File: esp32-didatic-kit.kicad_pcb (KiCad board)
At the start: 2 copper layers, 266 x 220 mm, 0 parts

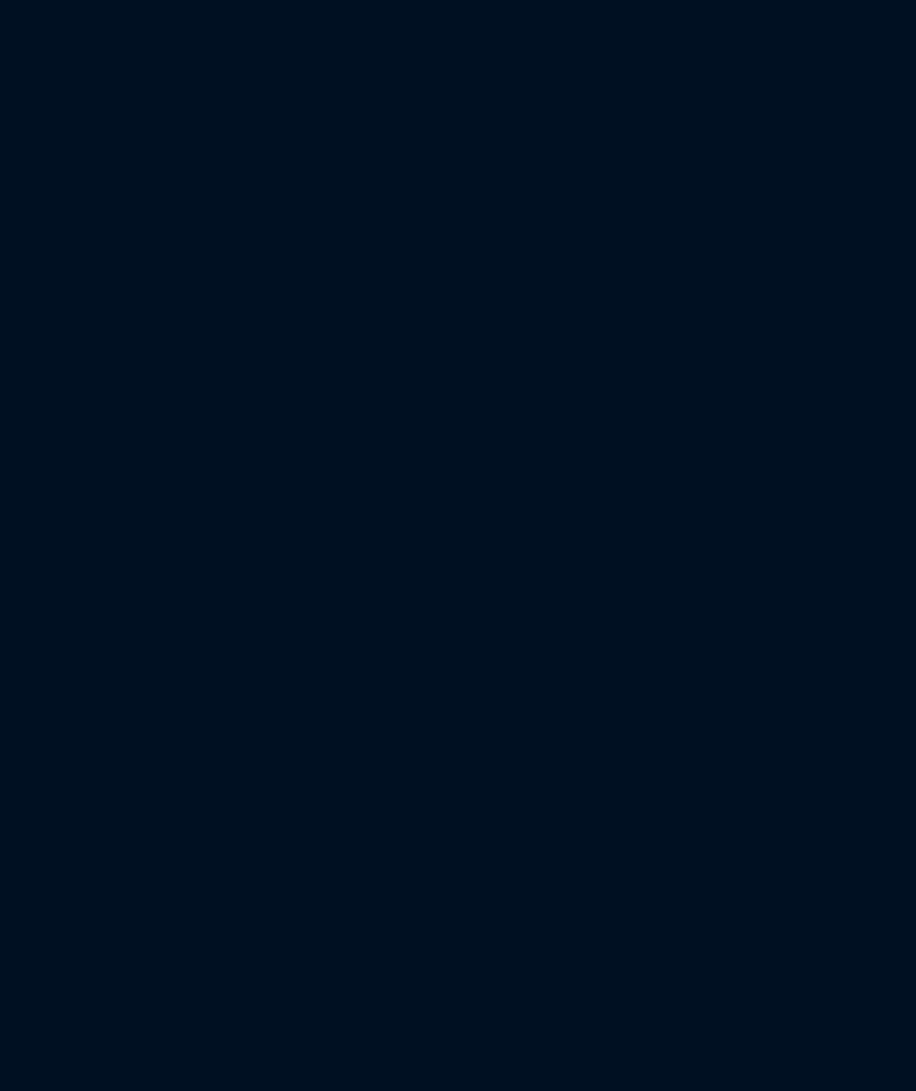
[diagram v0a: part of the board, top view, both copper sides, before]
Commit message: Use kicad footprints
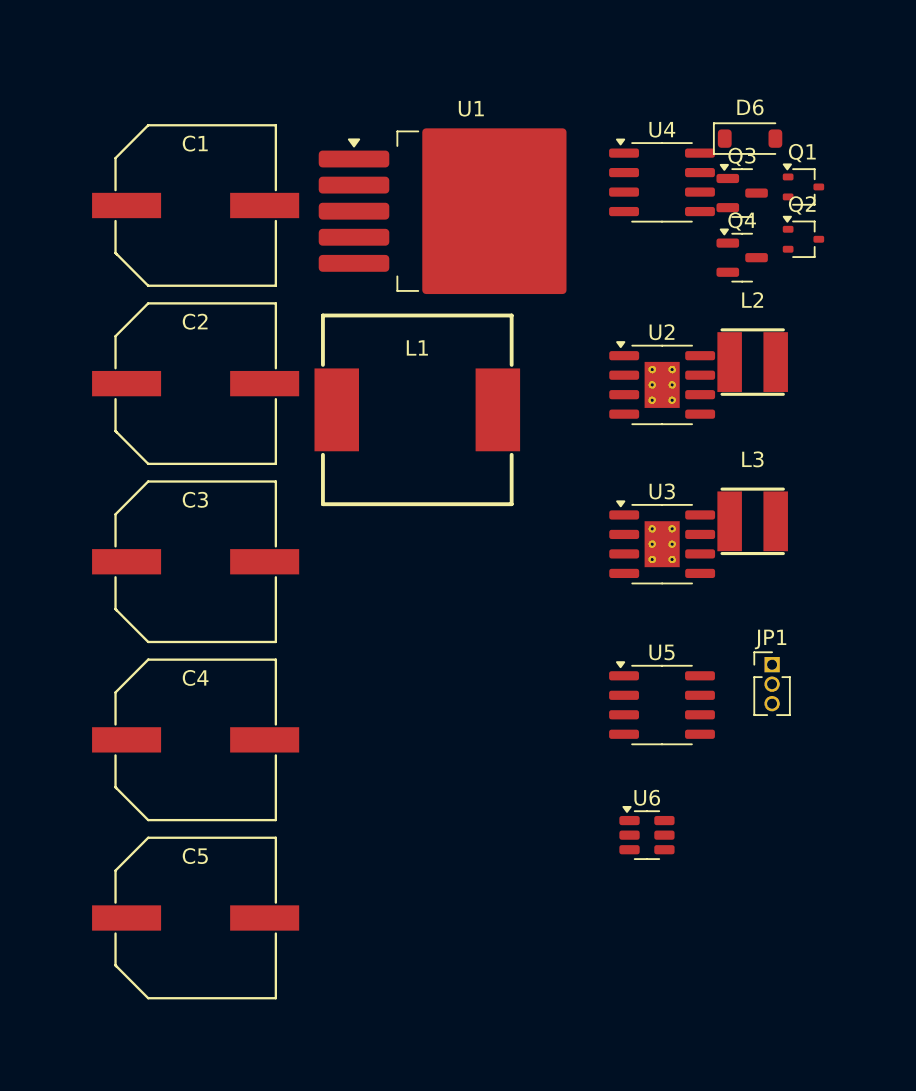
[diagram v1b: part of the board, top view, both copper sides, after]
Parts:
- added C1: 330uF, Passive:CAP-SMD_BD10.0-L10.3-W10.3-LS10.9-FD, F.Cu at (286.4, 61.3)
- added C2: 330uF, Passive:CAP-SMD_BD10.0-L10.3-W10.3-LS10.9-FD, F.Cu at (286.4, 72.9)
- added C3: 330uF, Passive:CAP-SMD_BD10.0-L10.3-W10.3-LS10.9-FD, F.Cu at (286.4, 84.5)
- added C4: 330uF, Passive:CAP-SMD_BD10.0-L10.3-W10.3-LS10.9-FD, F.Cu at (286.4, 96.1)
- added C5: 330uF, Passive:CAP-SMD_BD10.0-L10.3-W10.3-LS10.9-FD, F.Cu at (286.4, 107.7)
- added D6: PMEG3010ER,115, Diode_SMD:D_SOD-123, F.Cu at (322.6, 56.9)
- added JP1: REF-SEL, Connector_PinHeader_1.27mm:PinHeader_1x03_P1.27mm_Vertical, F.Cu at (324.0, 91.2)
- added L1: SMDRI127-221MT, Passive:IND-SMD_L12.3-W12.3_SMDRI127, F.Cu at (300.9, 74.6)
- added L2: 10uH, Passive:IND-SMD_L4.0-W4.0_FNR40XXS, F.Cu at (322.7, 71.5)
- added L3: 10uH, Passive:IND-SMD_L4.0-W4.0_FNR40XXS, F.Cu at (322.7, 81.9)
- added Q1: PDTC114EU,115, Package_TO_SOT_SMD:SOT-323_SC-70, F.Cu at (326.0, 60.1)
- added Q2: DMP2160UW-7, Package_TO_SOT_SMD:SOT-323_SC-70, F.Cu at (326.0, 63.5)
- added Q3: DMN2058U-7, Package_TO_SOT_SMD:SOT-23, F.Cu at (322.0, 60.5)
- added Q4: DMN2058U-7, Package_TO_SOT_SMD:SOT-23, F.Cu at (322.0, 64.7)
- added U1: LM2575-12BU, Package_TO_SOT_SMD:TO-263-5_TabPin3, F.Cu at (304.4, 61.6)
- added U2: ST1S10PHR, Package_SO:SOIC-8-1EP_3.9x4.9mm_P1.27mm_EP2.29x3mm_ThermalVias, F.Cu at (316.8, 73.0)
- added U3: ST1S10PHR, Package_SO:SOIC-8-1EP_3.9x4.9mm_P1.27mm_EP2.29x3mm_ThermalVias, F.Cu at (316.8, 83.3)
- added U4: MCP6H02T-E/SN, Package_SO:SOIC-8_3.9x4.9mm_P1.27mm, F.Cu at (316.8, 59.8)
- added U5: MCP1501-40E/SN, Package_SO:SOIC-8_3.9x4.9mm_P1.27mm, F.Cu at (316.8, 93.8)
- added U6: MCP4726A0T-E/CH, Package_TO_SOT_SMD:SOT-23-6, F.Cu at (315.8, 102.3)

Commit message: add MCU + output
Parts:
- added D10: LL4148, Diode_SMD:D_MiniMELF, F.Cu at (279.4, 182.0)
- added D11: LL4148, Diode_SMD:D_MiniMELF, F.Cu at (292.9, 178.7)
- added D12: LL4148, Diode_SMD:D_MiniMELF, F.Cu at (292.9, 182.0)
- added D13: LL4148, Diode_SMD:D_MiniMELF, F.Cu at (279.4, 197.6)
- added D14: LL4148, Diode_SMD:D_MiniMELF, F.Cu at (279.4, 200.9)
- added D15: LL4148, Diode_SMD:D_MiniMELF, F.Cu at (306.4, 178.7)
- added D16: LL4148, Diode_SMD:D_MiniMELF, F.Cu at (306.4, 182.0)
- added D17: LL4148, Diode_SMD:D_MiniMELF, F.Cu at (265.8, 178.7)
- added D18: LL4148, Diode_SMD:D_MiniMELF, F.Cu at (265.8, 182.0)
- added D19: LL4148, Diode_SMD:D_MiniMELF, F.Cu at (306.4, 197.6)
- added D20: LL4148, Diode_SMD:D_MiniMELF, F.Cu at (306.4, 200.9)
- added D21: LL4148, Diode_SMD:D_MiniMELF, F.Cu at (292.9, 197.6)
- added D22: LL4148, Diode_SMD:D_MiniMELF, F.Cu at (292.9, 200.9)
- added D23: LL4148, Diode_SMD:D_MiniMELF, F.Cu at (265.8, 197.6)
- added D24: LL4148, Diode_SMD:D_MiniMELF, F.Cu at (265.8, 200.9)
- added D8: LL4148, Diode_SMD:D_MiniMELF, F.Cu at (218.2, 151.2)
- added D9: LL4148, Diode_SMD:D_MiniMELF, F.Cu at (279.4, 178.7)
- added J2: Conn_02x05_Odd_Even, Connector_PinHeader_2.54mm:PinHeader_2x05_P2.54mm_Vertical, F.Cu at (264.9, 152.3)
- added J3: Conn_02x05_Odd_Even, Connector_PinHeader_2.54mm:PinHeader_2x05_P2.54mm_Vertical, F.Cu at (287.0, 152.3)
- added J4: Conn_02x05_Odd_Even, Connector_PinHeader_2.54mm:PinHeader_2x05_P2.54mm_Vertical, F.Cu at (287.0, 135.6)
- added J5: Conn_02x05_Odd_Even, Connector_PinHeader_2.54mm:PinHeader_2x05_P2.54mm_Vertical, F.Cu at (264.9, 135.6)
- added K1: G2RL-1, Relay_THT:Relay_SPDT_Omron_G2RL-1, F.Cu at (132.2, 35.1)
- added K10: G2RL-1, Relay_THT:Relay_SPDT_Omron_G2RL-1, F.Cu at (164.6, 100.0)
- added K11: G2RL-1, Relay_THT:Relay_SPDT_Omron_G2RL-1, F.Cu at (196.9, 100.0)
- added K12: G2RL-1, Relay_THT:Relay_SPDT_Omron_G2RL-1, F.Cu at (180.7, 67.5)
- added K13: G2RL-1, Relay_THT:Relay_SPDT_Omron_G2RL-1, F.Cu at (180.7, 100.0)
- added K14: G2RL-1, Relay_THT:Relay_SPDT_Omron_G2RL-1, F.Cu at (109.2, 69.7)
- added K15: G2RL-1, Relay_THT:Relay_SPDT_Omron_G2RL-1, F.Cu at (164.6, 67.5)
- added K16: G2RL-1, Relay_THT:Relay_SPDT_Omron_G2RL-1, F.Cu at (196.9, 67.5)
- added K2: G2RL-1, Relay_THT:Relay_SPDT_Omron_G2RL-1, F.Cu at (196.9, 35.1)
- added K3: G2RL-1, Relay_THT:Relay_SPDT_Omron_G2RL-1, F.Cu at (132.2, 67.5)
- added K4: G2RL-1, Relay_THT:Relay_SPDT_Omron_G2RL-1, F.Cu at (148.4, 67.5)
- added K5: G2RL-1, Relay_THT:Relay_SPDT_Omron_G2RL-1, F.Cu at (132.2, 100.0)
- added K6: G2RL-1, Relay_THT:Relay_SPDT_Omron_G2RL-1, F.Cu at (164.6, 35.1)
- added K7: G2RL-1, Relay_THT:Relay_SPDT_Omron_G2RL-1, F.Cu at (148.4, 35.1)
- added K8: G2RL-1, Relay_THT:Relay_SPDT_Omron_G2RL-1, F.Cu at (180.7, 35.1)
- added K9: G2RL-1, Relay_THT:Relay_SPDT_Omron_G2RL-1, F.Cu at (148.4, 100.0)
- added Q5: BSS138, Package_TO_SOT_SMD:SOT-23, F.Cu at (242.6, 198.3)
- added Q6: BSS138, Package_TO_SOT_SMD:SOT-23, F.Cu at (242.6, 202.9)
- added R30: 4K7, Resistor_SMD:R_0603_1608Metric, F.Cu at (238.2, 197.1)
- added R31: 4K7, Resistor_SMD:R_0603_1608Metric, F.Cu at (238.2, 199.7)
- added R32: 4K7, Resistor_SMD:R_0603_1608Metric, F.Cu at (238.2, 202.2)
- added R33: 4K7, Resistor_SMD:R_0603_1608Metric, F.Cu at (238.2, 204.7)
- added SW6: SW_DIP_x08, Button_Switch_SMD:SW_DIP_SPSTx08_Slide_6.7x21.88mm_W6.73mm_P2.54mm_LowProfile_JPin, F.Cu at (256.8, 49.7)
- added SW7: SW_DIP_x08, Button_Switch_SMD:SW_DIP_SPSTx08_Slide_6.7x21.88mm_W6.73mm_P2.54mm_LowProfile_JPin, F.Cu at (273.7, 49.8)
- added TB1: MKDSN 1,5/ 2-5,08, TerminalBlock_Phoenix:TerminalBlock_Phoenix_MKDS-1,5-2-5.08_1x02_P5.08mm_Horizontal, F.Cu at (239.7, 139.5)
- added TB10: MKDSN 1,5/ 2-5,08, TerminalBlock_Phoenix:TerminalBlock_Phoenix_MKDS-1,5-2-5.08_1x02_P5.08mm_Horizontal, F.Cu at (252.0, 188.0)
- added TB2: MKDSN 1,5/ 2-5,08, TerminalBlock_Phoenix:TerminalBlock_Phoenix_MKDS-1,5-2-5.08_1x02_P5.08mm_Horizontal, F.Cu at (239.7, 151.6)
- added TB3: MKDSN 1,5/ 2-5,08, TerminalBlock_Phoenix:TerminalBlock_Phoenix_MKDS-1,5-2-5.08_1x02_P5.08mm_Horizontal, F.Cu at (239.7, 163.8)
- added TB4: MKDSN 1,5/ 2-5,08, TerminalBlock_Phoenix:TerminalBlock_Phoenix_MKDS-1,5-2-5.08_1x02_P5.08mm_Horizontal, F.Cu at (239.7, 175.9)
- added TB5: MKDSN 1,5/ 2-5,08, TerminalBlock_Phoenix:TerminalBlock_Phoenix_MKDS-1,5-2-5.08_1x02_P5.08mm_Horizontal, F.Cu at (239.7, 188.0)
- added TB6: MKDSN 1,5/ 2-5,08, TerminalBlock_Phoenix:TerminalBlock_Phoenix_MKDS-1,5-2-5.08_1x02_P5.08mm_Horizontal, F.Cu at (252.0, 139.5)
- added TB7: MKDSN 1,5/ 2-5,08, TerminalBlock_Phoenix:TerminalBlock_Phoenix_MKDS-1,5-2-5.08_1x02_P5.08mm_Horizontal, F.Cu at (252.0, 151.6)
- added TB8: MKDSN 1,5/ 2-5,08, TerminalBlock_Phoenix:TerminalBlock_Phoenix_MKDS-1,5-2-5.08_1x02_P5.08mm_Horizontal, F.Cu at (252.0, 163.8)
- added TB9: MKDSN 1,5/ 2-5,08, TerminalBlock_Phoenix:TerminalBlock_Phoenix_MKDS-1,5-2-5.08_1x02_P5.08mm_Horizontal, F.Cu at (252.0, 175.9)
- added U10: HCPL2630SDVM, ICs:PDIP-8_L9.6-W6.4-P2.54-LS7.9-BL, F.Cu at (295.8, 171.9)
- added U11: HCPL2630SDVM, ICs:PDIP-8_L9.6-W6.4-P2.54-LS7.9-BL, F.Cu at (282.2, 190.8)
- added U12: HCPL2630SDVM, ICs:PDIP-8_L9.6-W6.4-P2.54-LS7.9-BL, F.Cu at (309.3, 171.9)
- added U13: HCPL2630SDVM, ICs:PDIP-8_L9.6-W6.4-P2.54-LS7.9-BL, F.Cu at (268.7, 171.9)
- added U14: HCPL2630SDVM, ICs:PDIP-8_L9.6-W6.4-P2.54-LS7.9-BL, F.Cu at (309.3, 190.8)
- added U15: HCPL2630SDVM, ICs:PDIP-8_L9.6-W6.4-P2.54-LS7.9-BL, F.Cu at (295.8, 190.8)
- added U16: HCPL2630SDVM, ICs:PDIP-8_L9.6-W6.4-P2.54-LS7.9-BL, F.Cu at (268.7, 190.8)
- added U17: PCF8574AT, Package_SO:SOIC-16W_7.5x10.3mm_P1.27mm, F.Cu at (298.3, 156.1)
- added U18: PCF8574AT, Package_SO:SOIC-16W_7.5x10.3mm_P1.27mm, F.Cu at (298.3, 139.3)
- added U19: PCF8574AT, Package_SO:SOIC-16W_7.5x10.3mm_P1.27mm, F.Cu at (276.2, 139.3)
- added U20: ULN2803A, Package_SO:SOIC-18W_7.5x11.6mm_P1.27mm, F.Cu at (112.3, 105.7)
- added U21: ULN2803A, Package_SO:SOIC-18W_7.5x11.6mm_P1.27mm, F.Cu at (102.6, 130.0)
- added U7: ESP32-WROVER-B, ICs:MODULE_ESP32-WROVER-B, F.Cu at (154.2, 172.0)
- added U8: PCF8574AT, Package_SO:SOIC-16W_7.5x10.3mm_P1.27mm, F.Cu at (276.2, 156.1)
- added U9: HCPL2630SDVM, ICs:PDIP-8_L9.6-W6.4-P2.54-LS7.9-BL, F.Cu at (282.2, 171.9)
- renumbered Q2 to Q1, Q1 to Q2, U6 to U5, U5 to U6
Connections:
- C1 pad 2: GND -> +5V
- C2 pad 2: GND -> +5V
- C3 pad 2: GND -> +5V
- C4 pad 2: GND -> +5V
- C5 pad 2: GND -> +5V
- Q2 pad 2: GND -> +5V
- Q3 pad 2: GND -> +5V
- Q4 pad 2: GND -> +5V
- U1 pad 3: GND -> +5V
- U2 pad 4: GND -> +5V
- U2 pad 5: GND -> +5V
- U2 pad 8: GND -> +5V
- U2 pad 9: GND -> +5V
- U3 pad 4: GND -> +5V
- U3 pad 5: GND -> +5V
- U3 pad 8: GND -> +5V
- U3 pad 9: GND -> +5V
- U4 pad 4: GND -> +5V
- U5 pad 2: GND -> +5V
- U6 pad 2: GND -> +5V
- U6 pad 4: GND -> +5V
- U6 pad 5: GND -> +5V
- U6 pad 6: GND -> +5V

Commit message: add mcu module + position components
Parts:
- removed Q6: BSS138, Package_TO_SOT_SMD:SOT-23
- removed R30, R31, R32, R33: 4K7, Resistor_SMD:R_0603_1608Metric
- added BOOT1: TL3342F160QG, Button_Switch_SMD:SW_SPST_TL3342, F.Cu at (486.6, 63.4)
- added C38: 30pF 50v, Capacitor_SMD:C_0603_1608Metric, F.Cu at (436.2, 129.5)
- added C39: 100nF, Capacitor_SMD:C_0603_1608Metric, F.Cu at (436.2, 132.0)
- added C40: 30pF 50v, Capacitor_SMD:C_0603_1608Metric, F.Cu at (436.2, 134.5)
- added C41: 30pF 50v, Capacitor_SMD:C_0603_1608Metric, F.Cu at (436.2, 137.0)
- added C48: 10nF, Capacitor_SMD:C_0603_1608Metric, F.Cu at (493.3, 64.5)
- added C49: 10nF, Capacitor_SMD:C_0603_1608Metric, F.Cu at (493.3, 67.0)
- added CON1: MIKROBUS_HOST_CONN, Connectors:MIKROBUS_HOST_CONN, F.Cu at (101.3, 100.1)
- added CON2: MIKROBUS_HOST_CONN, Connectors:MIKROBUS_HOST_CONN, F.Cu at (101.3, 129.7)
- added CON3: MIKROBUS_HOST_CONN, Connectors:MIKROBUS_HOST_CONN, F.Cu at (101.3, 160.1)
- added D41: BAT54J, Diode_SMD:D_SOD-323F, F.Cu at (448.9, 145.4)
- added J6: USB_C_Receptacle, Connector_USB:USB_C_Receptacle_GCT_USB4105-xx-A_16P_TopMnt_Horizontal, F.Cu at (440.1, 109.9)
- added J8: MCU_MODULE_CONN, Connectors:mcu_conn, F.Cu at (209.3, 136.4)
- added JP2: Jumper_3_Open, Connector_PinHeader_2.54mm:PinHeader_1x03_P2.54mm_Vertical, F.Cu at (484.1, 52.5)
- added JP3: Jumper_3_Open, Connector_PinHeader_2.54mm:PinHeader_1x03_P2.54mm_Vertical, F.Cu at (488.7, 52.5)
- added JP4: Jumper_3_Open, Connector_PinHeader_2.54mm:PinHeader_1x03_P2.54mm_Vertical, F.Cu at (493.3, 52.5)
- added JP5: Jumper_3_Open, Connector_PinHeader_2.54mm:PinHeader_1x03_P2.54mm_Vertical, F.Cu at (497.9, 52.5)
- added JP6: SolderJumper_2_Open, Jumper:SolderJumper-2_P1.3mm_Open_RoundedPad1.0x1.5mm, F.Cu at (448.9, 142.1)
- added Q7: 2N7002, Package_TO_SOT_SMD:SOT-23, F.Cu at (448.9, 69.9)
- added R103: 2K, Resistor_SMD:R_0603_1608Metric, F.Cu at (436.2, 139.5)
- added R104: 4K7, Resistor_SMD:R_0603_1608Metric, F.Cu at (436.2, 142.1)
- added R105: 4K7, Resistor_SMD:R_0603_1608Metric, F.Cu at (436.2, 144.6)
- added R106: 5K1, Resistor_SMD:R_0603_1608Metric, F.Cu at (444.7, 120.5)
- added R107: 5K1, Resistor_SMD:R_0603_1608Metric, F.Cu at (444.7, 123.0)
- added R35: 4K7, Resistor_SMD:R_0603_1608Metric, F.Cu at (448.4, 54.1)
- added R36: 4K7, Resistor_SMD:R_0603_1608Metric, F.Cu at (448.4, 56.6)
- added R37: 4K7, Resistor_SMD:R_0603_1608Metric, F.Cu at (448.4, 59.1)
- added R38: 4K7, Resistor_SMD:R_0603_1608Metric, F.Cu at (448.4, 61.6)
- added RST1: TL3342F160QG, Button_Switch_SMD:SW_SPST_TL3342, F.Cu at (486.6, 70.5)
- added SW2: TDS08SGRNTU04, Connectors:TDS08SGRNTU04, F.Cu at (315.6, 92.7)
- added SW3: TDS08SGRNTU04, Connectors:TDS08SGRNTU04, F.Cu at (315.7, 147.8)
- added SW4: TDS08SGRNTU04, Connectors:TDS08SGRNTU04, F.Cu at (274.9, 149.1)
- added SW5: TDS08SGRNTU04, Connectors:TDS08SGRNTU04, F.Cu at (272.7, 92.5)
- added TB11: MKDSN 1,5/ 2-5,08, TerminalBlock_Phoenix:TerminalBlock_Phoenix_MKDS-1,5-2-5.08_1x02_P5.08mm_Horizontal, F.Cu at (441.8, 134.5)
- added TB13: MKDSN 1,5/ 2-5,08, TerminalBlock_Phoenix:TerminalBlock_Phoenix_MKDS-1,5-2-5.08_1x02_P5.08mm_Horizontal, F.Cu at (110.3, 238.9)
- added TB14: MKDSN 1,5/ 2-5,08, TerminalBlock_Phoenix:TerminalBlock_Phoenix_MKDS-1,5-2-5.08_1x02_P5.08mm_Horizontal, F.Cu at (227.4, 238.9)
- added TB15: MKDSN 1,5/ 2-5,08, TerminalBlock_Phoenix:TerminalBlock_Phoenix_MKDS-1,5-2-5.08_1x02_P5.08mm_Horizontal, F.Cu at (122.0, 238.9)
- added TB16: MKDSN 1,5/ 2-5,08, TerminalBlock_Phoenix:TerminalBlock_Phoenix_MKDS-1,5-2-5.08_1x02_P5.08mm_Horizontal, F.Cu at (239.1, 238.9)
- added TB17: MKDSN 1,5/ 2-5,08, TerminalBlock_Phoenix:TerminalBlock_Phoenix_MKDS-1,5-2-5.08_1x02_P5.08mm_Horizontal, F.Cu at (133.7, 238.9)
- added TB18: MKDSN 1,5/ 2-5,08, TerminalBlock_Phoenix:TerminalBlock_Phoenix_MKDS-1,5-2-5.08_1x02_P5.08mm_Horizontal, F.Cu at (250.8, 238.9)
- added TB19: MKDSN 1,5/ 2-5,08, TerminalBlock_Phoenix:TerminalBlock_Phoenix_MKDS-1,5-2-5.08_1x02_P5.08mm_Horizontal, F.Cu at (145.4, 238.9)
- added TB20: MKDSN 1,5/ 2-5,08, TerminalBlock_Phoenix:TerminalBlock_Phoenix_MKDS-1,5-2-5.08_1x02_P5.08mm_Horizontal, F.Cu at (262.5, 238.9)
- added TB21: MKDSN 1,5/ 2-5,08, TerminalBlock_Phoenix:TerminalBlock_Phoenix_MKDS-1,5-2-5.08_1x02_P5.08mm_Horizontal, F.Cu at (157.1, 238.9)
- added TB22: MKDSN 1,5/ 2-5,08, TerminalBlock_Phoenix:TerminalBlock_Phoenix_MKDS-1,5-2-5.08_1x02_P5.08mm_Horizontal, F.Cu at (274.2, 238.9)
- added TB23: MKDSN 1,5/ 2-5,08, TerminalBlock_Phoenix:TerminalBlock_Phoenix_MKDS-1,5-2-5.08_1x02_P5.08mm_Horizontal, F.Cu at (168.8, 238.9)
- added TB24: MKDSN 1,5/ 2-5,08, TerminalBlock_Phoenix:TerminalBlock_Phoenix_MKDS-1,5-2-5.08_1x02_P5.08mm_Horizontal, F.Cu at (285.9, 238.9)
- added TB25: MKDSN 1,5/ 2-5,08, TerminalBlock_Phoenix:TerminalBlock_Phoenix_MKDS-1,5-2-5.08_1x02_P5.08mm_Horizontal, F.Cu at (180.5, 238.9)
- added TB26: MKDSN 1,5/ 2-5,08, TerminalBlock_Phoenix:TerminalBlock_Phoenix_MKDS-1,5-2-5.08_1x02_P5.08mm_Horizontal, F.Cu at (297.6, 238.9)
- added TB27: MKDSN 1,5/ 2-5,08, TerminalBlock_Phoenix:TerminalBlock_Phoenix_MKDS-1,5-2-5.08_1x02_P5.08mm_Horizontal, F.Cu at (192.2, 238.9)
- added TB28: MKDSN 1,5/ 2-5,08, TerminalBlock_Phoenix:TerminalBlock_Phoenix_MKDS-1,5-2-5.08_1x02_P5.08mm_Horizontal, F.Cu at (309.3, 238.9)
- added TB29: MKDSN 1,5/ 2-5,08, TerminalBlock_Phoenix:TerminalBlock_Phoenix_MKDS-1,5-2-5.08_1x02_P5.08mm_Horizontal, F.Cu at (332.7, 238.9)
- added TB30: MKDSN 1,5/ 2-5,08, TerminalBlock_Phoenix:TerminalBlock_Phoenix_MKDS-1,5-2-5.08_1x02_P5.08mm_Horizontal, F.Cu at (321.0, 238.9)
- added TB31: MKDSN 1,5/ 2-5,08, TerminalBlock_Phoenix:TerminalBlock_Phoenix_MKDS-1,5-2-5.08_1x02_P5.08mm_Horizontal, F.Cu at (203.9, 238.9)
- added TB32: MKDSN 1,5/ 2-5,08, TerminalBlock_Phoenix:TerminalBlock_Phoenix_MKDS-1,5-2-5.08_1x02_P5.08mm_Horizontal, F.Cu at (215.7, 238.9)
- added U22: SN65HVD231, Package_SO:SOIC-8_3.9x4.9mm_P1.27mm, F.Cu at (442.5, 143.7)
- added U23: USBLC6-2SC6, Package_TO_SOT_SMD:SOT-23-6, F.Cu at (445.2, 117.0)
- added U24: CH340G, Package_SO:SOIC-16_3.9x9.9mm_P1.27mm, F.Cu at (438.4, 120.5)
- Q5: value BSS138 -> 2N7002
- moved U7 330.7 mm to (476.8, 245.1)
- moved D8 290.6 mm to (494.6, 61.6)
- moved Q5 245.4 mm to (448.9, 65.2)
- moved TB10 227.7 mm to (83.0, 35.4)
- moved D19 226.6 mm to (129.6, 55.9)
- moved D20 226.6 mm to (129.6, 59.2)
- moved U14 226.6 mm to (132.4, 49.1)
- moved D21 225.2 mm to (117.8, 55.9)
- moved D22 225.2 mm to (117.8, 59.2)
- moved U15 225.2 mm to (120.7, 49.1)
- moved D23 213.2 mm to (106.1, 56.3)
- moved D24 213.2 mm to (106.1, 59.6)
- moved U16 213.2 mm to (109.0, 49.5)
- moved TB9 210.9 mm to (94.7, 35.4)
- moved K14 200.5 mm to (271.0, 188.2)
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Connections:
- net /MCU/GPIO25 renamed /MCU/VSPI.CS0
- net /MCU/GPIO26 renamed /MCU/VSPI.CS1
- net /MCU/GPIO32 renamed /MCU/IO32
- net /MCU/GPIO33 renamed /MCU/IO33
- net /MCU/JTAG.TDI renamed Net-(D8-A)
- net /MCU/SERIAL0.IO0 renamed /USB-SERIAL/DBG_UART.DTR
- K10 pad 12: /IO/Output PortD/Relay Circuit1/NC -> /IO/Output PortD/NC1
- K10 pad 14: /IO/Output PortD/Relay Circuit1/NO -> /IO/Output PortD/NO1
- K2 pad 12: /IO/Output PortC/Relay Circuit1/NC -> /IO/Output PortC/NC1
- K2 pad 14: /IO/Output PortC/Relay Circuit1/NO -> /IO/Output PortC/NO1
- Q5 pad 2: /IO/IO_SDA -> /MCU/I2C0.SCL
- Q5 pad 3: /IO/I2C.SDA -> /IO/I2C.SCL
- U7 pad 12: /MCU/GPIO27 -> unconnected-(U7-IO27-Pad12)
- U7 pad 13: /MCU/JTAG.TMS -> Net-(JP3-C)
- U7 pad 16: /MCU/JTAG.TCK -> Net-(JP4-C)
- U7 pad 23: /MCU/JTAG.TDO -> /MCU/IO15
- U7 pad 24: /MCU/GPIO2 -> unconnected-(U7-IO2-Pad24)
- U7 pad 26: /MCU/GPIO4 -> /Can Bus/CAN.RX
- U7 pad 29: /MCU/GPIO5 -> /Can Bus/CAN.TX
- U7 pad 3: /MCU/SERIAL0.EN -> /USB-SERIAL/DBG_UART.RTS
- U7 pad 30: /MCU/GPIO18 -> /MCU/VSPI.SCK
- U7 pad 31: /MCU/GPIO19 -> /MCU/VSPI.MISO
- U7 pad 33: /MCU/GPIO21 -> /MCU/I2C0.SDA
- U7 pad 34: /MCU/SERIAL0.RX -> /USB-SERIAL/DBG_UART.TX
- U7 pad 35: /MCU/SERIAL0.TX -> /USB-SERIAL/DBG_UART.RX
- U7 pad 36: /MCU/GPIO22 -> /MCU/I2C0.SCL
- U7 pad 37: /MCU/GPIO23 -> /MCU/VSPI.MOSI
